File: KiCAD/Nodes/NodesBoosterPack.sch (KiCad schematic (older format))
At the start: 7 parts, among them U1 NRF24L01+, U2 LAUNCHPAD

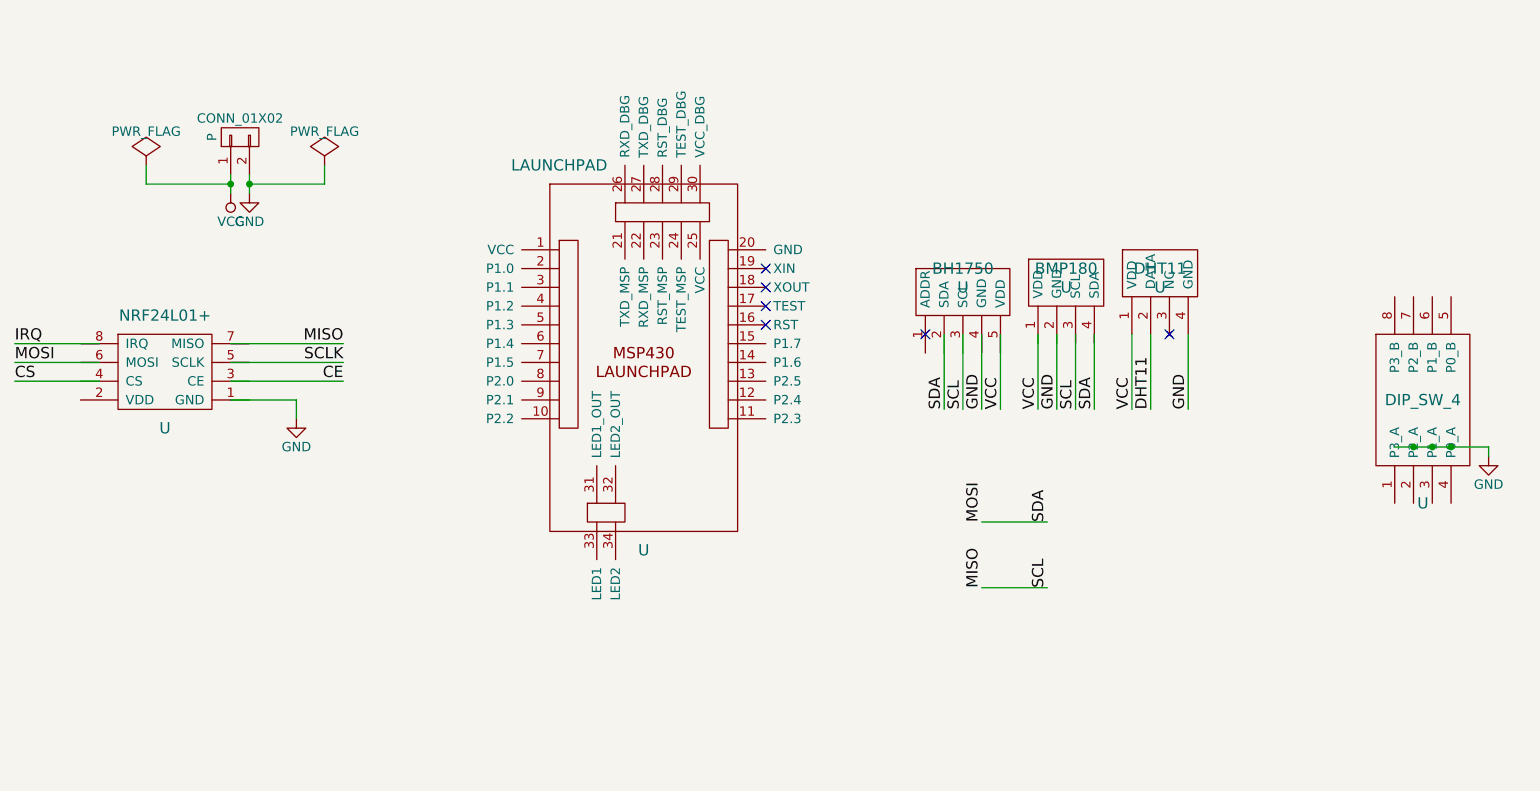
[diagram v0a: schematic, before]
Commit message: Added PCB design for WSN Nodes
Preliminar final design
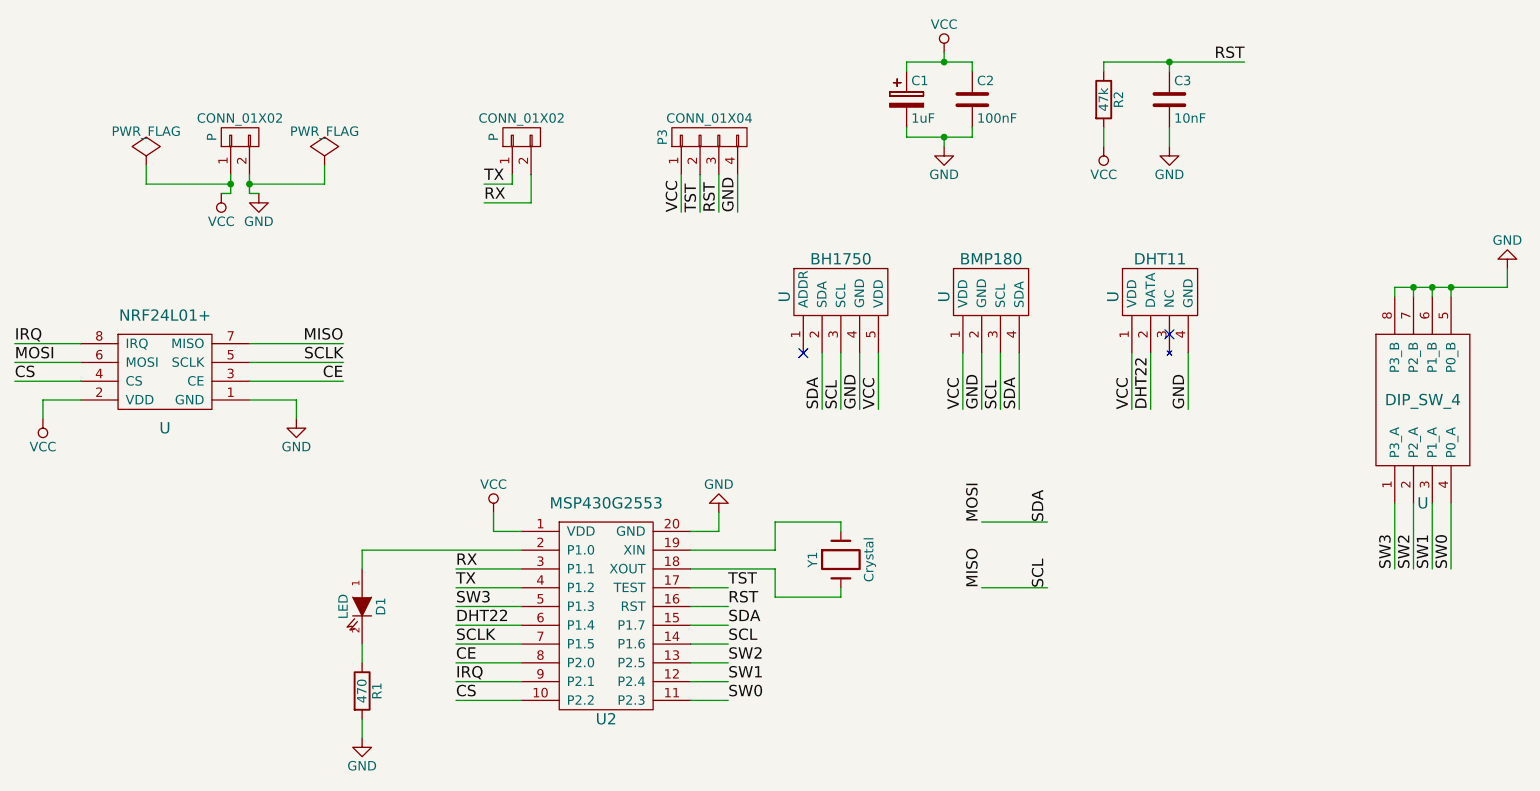
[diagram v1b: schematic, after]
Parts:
- removed U2: LAUNCHPAD, symbol LAUNCHPAD
- added C1: 1uF, Capacitors_Tantalum_SMD:TantalC_SizeA_EIA-3216_HandSoldering, symbol CP
- added C2: 100nF, Capacitors_SMD:C_1206_HandSoldering, symbol C
- added C3: 10nF, Capacitors_SMD:C_1206_HandSoldering, symbol C
- added D1: LED, LEDs:LED-1206, symbol LED
- added P2: CONN_01X02, Pin_Headers:Pin_Header_Straight_2x01, symbol CONN_01X02
- added P3: CONN_01X04, Pin_Headers:Pin_Header_Straight_1x04, symbol CONN_01X04
- added R1: 470, Resistors_SMD:R_1206_HandSoldering, symbol R
- added R2: 47k, Resistors_SMD:R_1206_HandSoldering, symbol R
- added U2: MSP430G2553, Housings_DIP:DIP-20__300, symbol MSP430G2553
- added Y1: Crystal, Crystals:Crystal_Round_Horizontal_3mm_BigPad, symbol Crystal
- P1: renamed from P?; footprint (none) -> Libraries:BAT_HOLDER_2xAA
- U1: footprint (none) -> Pin_Headers:Pin_Header_Straight_2x04
- U3: renamed from U?; footprint (none) -> Pin_Headers:Pin_Header_Straight_1x05
- U4, U5: renamed from U?; footprint (none) -> Pin_Headers:Pin_Header_Straight_1x04
- U6: renamed from U?; footprint (none) -> Housings_DIP:DIP-8__300
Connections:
- net labels added: DHT22, RST, RX, SW0, SW1, SW2, SW3, TST, TX
- net labels removed: DHT11
- wire segments 29 -> 93
- no-connect marks 6 -> 2
